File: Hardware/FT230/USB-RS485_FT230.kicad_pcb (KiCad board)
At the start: 2 copper layers, 59 x 22.5 mm, 39 parts, among them J2 7-pin con, J3 5 LVL 3.3, J6 USB_C_Receptacle_USB2.0_16P, Q1 BC857, U1 CH340G, U2 SN75176AD, U3 AMS1117-3.3, U4 DC-DC, U5 EL817, U6 EL817, Y1 12MHz

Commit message: FT230 PCB - in progress
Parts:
- removed Y1: 12MHz, Crystal:Crystal_SMD_3225-4Pin_3.2x2.5mm
- added C5: 100nF, Capacitor_SMD:C_0805_2012Metric, F.Cu at (68.9, 99.9)
- added R7: 10k, Resistor_SMD:R_0805_2012Metric, F.Cu at (71.5, 91.4)
- added R8: 1k, Resistor_SMD:R_0805_2012Metric, F.Cu at (75.8, 96.3)
- C1: value 12pF -> 4.7uF
- C2: value 12pF -> 47pF
- C4: value 100nF -> 47pF
- J2: renamed from J3; value 5 LVL 3.3 -> 3.3 LVL 5
- R1: value 10k -> 27R
- R2: value 1k -> 27R
- U1: value CH340G -> FT230XQ; footprint Package_SO:SOIC-16_3.9x9.9mm_P1.27mm -> Package_DFN_QFN:QFN-16-1EP_4x4mm_P0.65mm_EP2.1x2.1mm
- moved C4 12.0 mm to (65.9, 98.5), turned to 180 degrees
- moved R2 12.0 mm to (65.9, 94.2), turned to 180 degrees
- moved R1 10.5 mm to (65.9, 96.3), turned to 180 degrees
- moved C2 9.04 mm to (65.9, 92.0), turned to 180 degrees
- moved D2 8.06 mm to (71.5, 89.2)
- moved L1 5.46 mm to (75.7, 85.7), turned to 0 degrees
- moved D1 5.33 mm to (73.5, 99.9), turned to -90 degrees
- moved C7 3.48 mm to (77.0, 89.0), turned to 90 degrees
- moved R6 3.15 mm to (74.4, 90.6), turned to 90 degrees
- moved C3 2.63 mm to (65.9, 89.8), turned to 0 degrees
- moved U1 2.45 mm to (70.8, 95.2), turned to -90 degrees
- moved R5 2.41 mm to (75.8, 99.9), turned to -90 degrees
- moved C1 1.44 mm to (71.2, 99.9)
- renumbered C6 to C10, C7 to C6, C8 to C7, C9 to C8, C5 to C9, D4 to D1, D3 to D2, D2 to D3, D1 to D4, J6 to J1, J2 to J3, R12 to R10, R7 to R11, R11 to R12, R9 to R13, R10 to R14, R13 to R15, R6 to R16, R14 to R3, R15 to R4, R3 to R5, R4 to R6, R8 to R9, U5 to U2, U6 to U3, U3 to U5, U2 to U6
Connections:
- C1 pad 2: Net-(U1-XI) -> +5V_USB
- C2 pad 1: GND1 -> Net-(U1-USBDP)
- C2 pad 2: Net-(U1-XO) -> GND1
- C3 pad 1: Net-(U1-V3) -> +5V_USB
- C3 pad 2: +5V_USB -> GND1
- C4 pad 1: +5V_USB -> Net-(U1-USBDM)
- D1 pad 1: Net-(D4-K) -> Net-(D1-K)
- D2 pad 1: Net-(D3-K) -> Net-(D2-K)
- J1 pad A6: Net-(U1-UD+) -> Net-(J1-D+-PadA6)
- J1 pad A7: Net-(U1-UD-) -> Net-(J1-D--PadA7)
- J1 pad B6: Net-(U1-UD+) -> Net-(J1-D+-PadA6)
- J1 pad B7: Net-(U1-UD-) -> Net-(J1-D--PadA7)
- R1 pad 1: +5V_USB -> Net-(U1-USBDM)
- R1 pad 2: Net-(D4-K) -> Net-(J1-D--PadA7)
- R2 pad 1: +5V_USB -> Net-(U1-USBDP)
- R2 pad 2: Net-(R2-Pad2) -> Net-(J1-D+-PadA6)
- R5 pad 1: +5V_USB -> VCCIO
- R6 pad 1: +5V_USB -> VCCIO
- U1 pad 1: GND1 -> VCCIO
- U1 pad 10: unconnected-(U1-~{DSR}-Pad10) -> +5V_USB
- U1 pad 11: unconnected-(U1-~{RI}-Pad11) -> Net-(D1-K)
- U1 pad 13: unconnected-(U1-~{DTR}-Pad13) -> GND1
- U1 pad 15: unconnected-(U1-R232-Pad15) -> Net-(U1-TXD)
- U1 pad 16: +5V_USB -> unconnected-(U1-~{RTS}-Pad16)
- U1 pad 2: Net-(D3-K) -> Net-(U1-RXD)
- U1 pad 3: Net-(D4-K) -> GND1
- U1 pad 4: Net-(U1-V3) -> unconnected-(U1-~{CTS}-Pad4)
- U1 pad 5: Net-(U1-UD+) -> Net-(D2-K)
- U1 pad 6: Net-(U1-UD-) -> Net-(U1-USBDP)
- U1 pad 7: Net-(U1-XI) -> Net-(U1-USBDM)
- U1 pad 8: Net-(U1-XO) -> VCCIO
- U1 pad 9: unconnected-(U1-~{CTS}-Pad9) -> VCCIO
- U2 pad 1: Net-(R2-Pad2) -> Net-(R8-Pad2)
- U2 pad 2: Net-(D3-K) -> Net-(U1-TXD)
- U3 pad 4: Net-(D4-K) -> Net-(U1-RXD)
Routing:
- net Net-(D4-K): track 38.4 -> 0.00 mm
- net Net-(D3-K): track 26.7 -> 0.00 mm
- net GND1: track 89.3 -> 64.6 mm, vias 10 -> 9
- net VCCIO: track 0.00 -> 24.0 mm, vias 0 -> 2
- net +5V_USB: track 52.4 -> 33.4 mm
- net Net-(U1-RXD): track 0.00 -> 16.7 mm
- net Net-(U1-TXD): track 0.00 -> 13.5 mm
- net Net-(U1-V3): track 9.47 -> 0.00 mm
- net Net-(U1-XO): track 8.45 -> 0.00 mm
- net Net-(R8-Pad2): track 0.00 -> 7.80 mm
- net Net-(U1-XI): track 7.73 -> 0.00 mm
- net Net-(U1-UD-): track 7.16 -> 0.00 mm, vias 2 -> 0
- net Net-(U1-UD+): track 6.73 -> 0.00 mm
- net Net-(J1-D--PadA7): track 0.00 -> 6.21 mm, vias 0 -> 2
- net Net-(D2-K): track 0.00 -> 5.86 mm
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
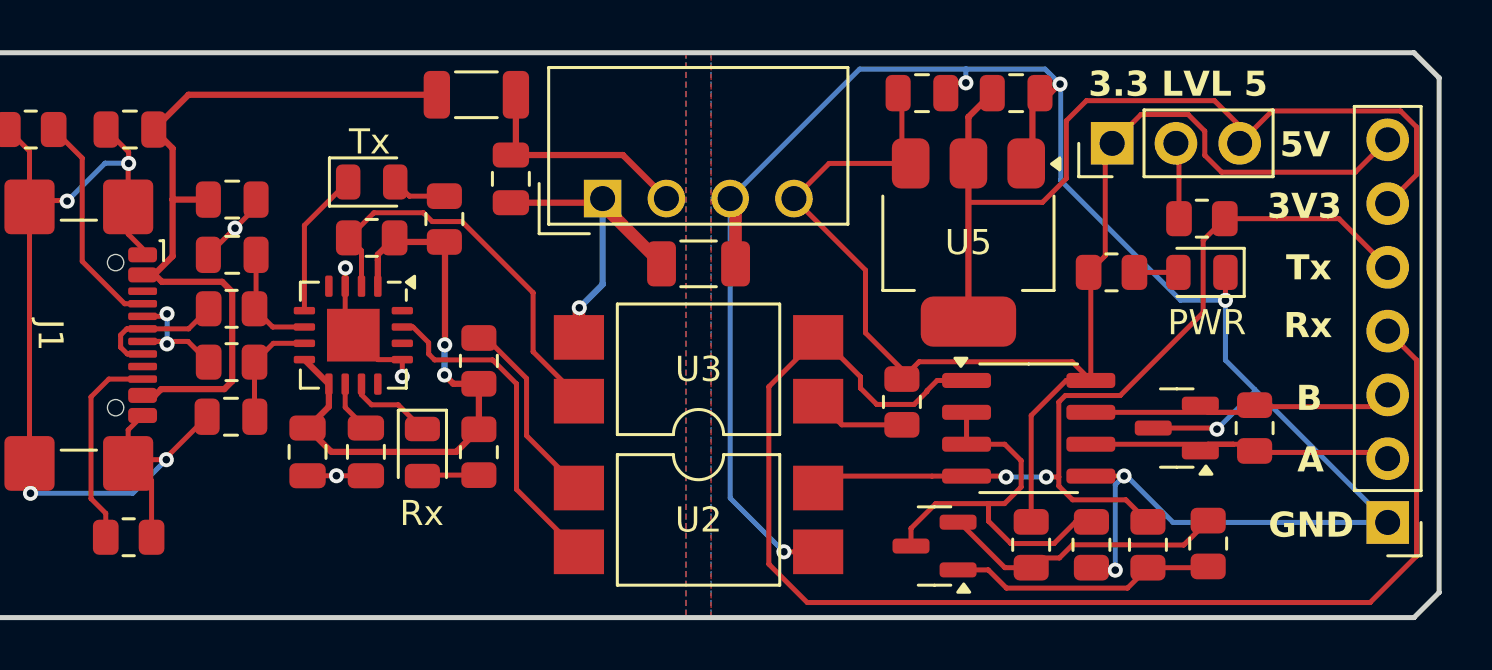
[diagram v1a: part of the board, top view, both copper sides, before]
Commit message: FT230 BOM and fix
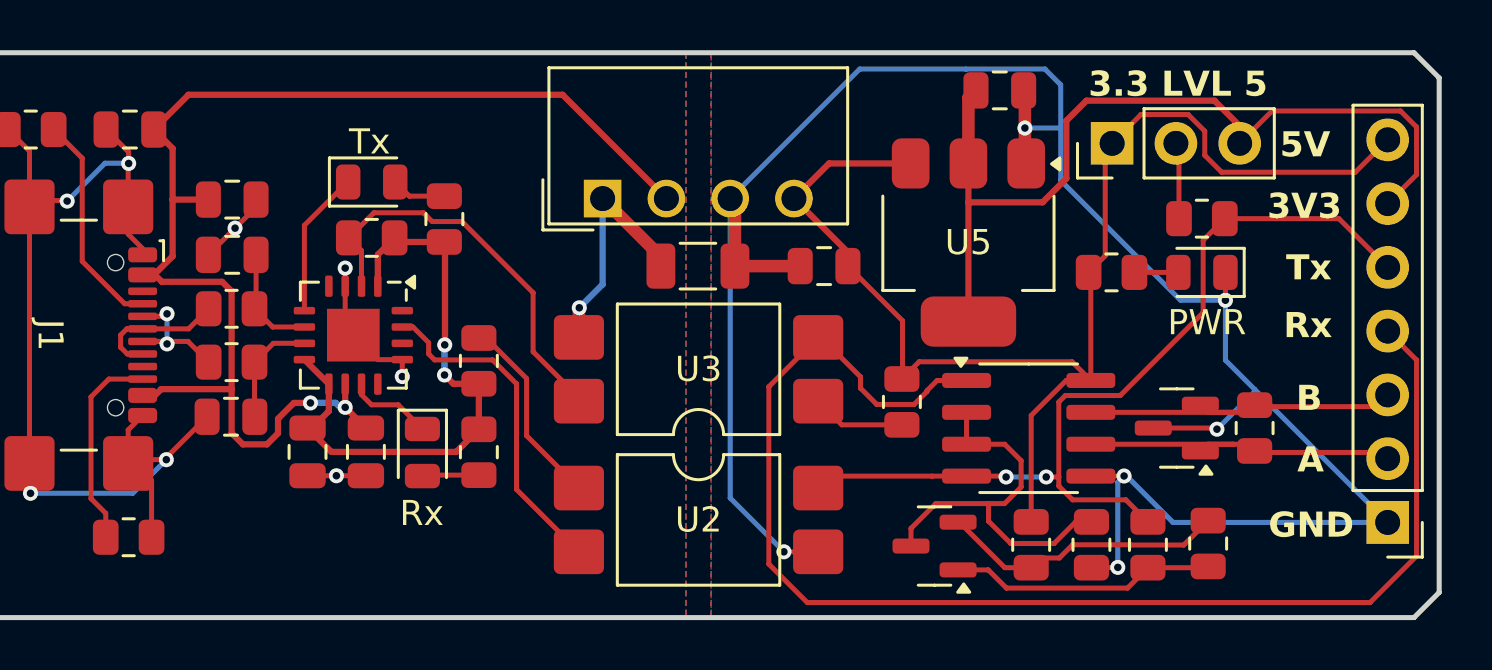
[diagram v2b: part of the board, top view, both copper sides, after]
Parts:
- removed C10: 22uF, Capacitor_SMD:C_0805_2012Metric
- removed L1: 6.8uH, Inductor_SMD:L_1206_3216Metric
- C7: value 4.7uF -> 270pF/2kV; footprint Capacitor_SMD:C_0805_2012Metric -> Capacitor_SMD:C_1206_3216Metric
- C8: value 270pF/2kV -> 10uF; footprint Capacitor_SMD:C_1206_3216Metric -> Capacitor_SMD:C_0805_2012Metric
- C9: value 10uF -> 22uF
- U6: value SN75176AD -> SN75176
- moved C7 8.22 mm to (84.5, 92.5), turned to 0 degrees
- moved C8 5.00 mm to (89.5, 92.5)
- moved C9 3.10 mm to (96.5, 85.5)
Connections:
- C7 pad 2: Net-(U4-+Vin) -> GND2
- C8 pad 1: GND1 -> GND2
- C8 pad 2: GND2 -> +5V_OUT
- C9 pad 2: +5V_OUT -> +3.3V_OUT
- U4 pad 2: Net-(U4-+Vin) -> +5V_USB
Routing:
- net +5V_USB: track 33.4 -> 52.0 mm, vias 0 -> 2
- net Net-(U4-+Vin): track 9.40 -> 0.00 mm
- net GND1: track 64.6 -> 60.9 mm
- net +5V_OUT: track 55.9 -> 52.9 mm
- net GND2: track 87.3 -> 88.8 mm, vias 7 -> 6
- net +3.3V_OUT: track 36.7 -> 35.5 mm

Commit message: FT230 gerbers export
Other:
- board text added: "USB-UART/RS485 (GALVANIC ISOLATION)"
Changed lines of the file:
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@@
+		)
+	)
+	(gr_text "USB-UART/RS485 (GALVANIC ISOLATION)"
+		(at 87.45 86.45 0)
+		(layer "B.SilkS")
+		(effects
+			(font
+				(size 1 1)
+				(thickness 0.25)
+				(bold yes)
+			)
+			(justify left bottom mirror)
 		)
 	)

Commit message: -opto +Adum & 1.8
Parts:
- removed C9: 22uF, Capacitor_SMD:C_0805_2012Metric
- removed J2: 3.3 LVL 5, Connector_PinHeader_2.54mm:PinHeader_1x03_P2.54mm_Vertical
- removed R7: 10k, Resistor_SMD:R_0805_2012Metric
- removed R8, R9: 1k, Resistor_SMD:R_0805_2012Metric
- removed U2, U3: EL817, Package_DIP:SMDIP-4_W9.53mm
- added C10: 100nF, Capacitor_SMD:C_0805_2012Metric, F.Cu at (62.2, 77.1)
- added J4: Conn_02x03_Odd_Even, Connector_PinHeader_1.00mm:PinHeader_2x03_P1.00mm_Vertical, F.Cu at (57.3, 77.1)
- added U7: ADuM121N, Package_SO:SOIC-8_3.9x4.9mm_P1.27mm, F.Cu at (59.9, 72.4)
- D1: value Rx -> Tx
- D2: value Tx -> Rx
- U5: value AMS1117-3.3 -> AP7345D-1833RH4-7; footprint Package_TO_SOT_SMD:SOT-223-3_TabPin2 -> AP7345D-1833:AP7345D1833RH47
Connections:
- C7 pad 2: GND2 -> Net-(U4--Vout)
- C8 pad 1: GND2 -> Net-(U4--Vout)
- R11 pad 2: Net-(J2-Pin_2) -> unconnected-(R11-Pad2)
- U4 pad 3: GND2 -> Net-(U4--Vout)
- U5 pad 2: +3.3V_OUT -> +1.8V
- U5 pad 3: +5V_OUT -> +3.3V
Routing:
- net (no net): track 0.00 -> 11.5 mm
- net Net-(R8-Pad2): track 7.80 -> 0.00 mm
- net Net-(R9-Pad2): track 3.73 -> 0.00 mm
- net unconnected-(R11-Pad2): track 0.00 -> 3.05 mm
- net Net-(J2-Pin_2): track 3.05 -> 0.00 mm

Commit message: schematics change
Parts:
- removed J3: 7-pin con, Connector_PinHeader_2.54mm:PinHeader_1x07_P2.54mm_Vertical
- removed Q1: BC857, Package_TO_SOT_SMD:SOT-23
- removed R10, R14: 100R, Resistor_SMD:R_0805_2012Metric
- removed R11, R12, R13: 10k, Resistor_SMD:R_0805_2012Metric
- removed R15: 120R, Resistor_SMD:R_0805_2012Metric
- removed R16: 1k, Resistor_SMD:R_0805_2012Metric
- removed U6: SN75176, Package_SO:SOIC-8_3.9x4.9mm_P1.27mm
- removed U7: ADuM121N, Package_SO:SOIC-8_3.9x4.9mm_P1.27mm
- added C11: 10uF, Capacitor_SMD:C_0805_2012Metric, F.Cu at (83.0, 58.0)
- added C12: 100nF, Capacitor_SMD:C_0805_2012Metric, F.Cu at (83.0, 61.0)
- added C13: 100nF, Capacitor_SMD:C_0805_2012Metric, F.Cu at (83.0, 64.0)
- added C14: 100nF, Capacitor_SMD:C_0805_2012Metric, F.Cu at (83.0, 67.0)
- added C15: 100nF, Capacitor_SMD:C_0805_2012Metric, F.Cu at (83.0, 70.0)
- added C9: 270pF/2kV, Capacitor_SMD:C_1206_3216Metric, F.Cu at (95.7, 58.2)
- added J2: 7-pin con, Connector_PinHeader_2.54mm:PinHeader_1x07_P2.54mm_Vertical, F.Cu at (72.9, 56.8)
- added R7: 120R, Resistor_SMD:R_0805_2012Metric, F.Cu at (95.9, 71.3)
- added R8: 1k, Resistor_SMD:R_0805_2012Metric, F.Cu at (95.9, 74.3)
- added U2: ADuM121N, Package_SO:SOIC-8_3.9x4.9mm_P1.27mm, F.Cu at (113.6, 63.6)
- added U3: DC-DC, Converter_DCDC:Converter_DCDC_TRACO_TEA1-xxxx_THT, F.Cu at (110.2, 59.8)
- C7: value 270pF/2kV -> 100nF; footprint Capacitor_SMD:C_1206_3216Metric -> Capacitor_SMD:C_0805_2012Metric
- C8: value 10uF -> 100nF
- J4: value Conn_02x03_Odd_Even -> Conn_02x04_Odd_Even
- U4: value DC-DC -> ISO3082DW; footprint Converter_DCDC:Converter_DCDC_TRACO_TEA1-xxxx_THT -> Package_SO:SOIC-16W_7.5x10.3mm_P1.27mm
- moved C7 52.2 mm to (135.7, 82.5)
- moved U4 37.4 mm to (113.6, 72.0), turned to 0 degrees
- moved C8 36.9 mm to (126.3, 90.7)
- moved U5 30.7 mm to (125.2, 84.5)
- moved D3 23.9 mm to (118.8, 80.6)
- moved D4 14.5 mm to (118.5, 88.9)
- moved J4 12.4 mm to (58.0, 64.7)
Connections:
- C10 pad 1: GND1 -> +V_OUT
- C10 pad 2: VCCIO -> GND2
- C7 pad 2: Net-(U4--Vout) -> Net-(U4-Vcc1)
- C8 pad 1: Net-(U4--Vout) -> GND1
- C8 pad 2: +5V_OUT -> VCCIO
- J4 pad 1: unconnected-(J4-Pin_1-Pad1) -> +1.8V_ISO
- J4 pad 2: unconnected-(J4-Pin_2-Pad2) -> +V_OUT
- J4 pad 3: unconnected-(J4-Pin_3-Pad3) -> +3.3V_ISO
- J4 pad 4: unconnected-(J4-Pin_4-Pad4) -> +V_OUT
- J4 pad 5: unconnected-(J4-Pin_5-Pad5) -> +5V_ISO
- J4 pad 6: unconnected-(J4-Pin_6-Pad6) -> +V_OUT
- U1 pad 11: Net-(D1-K) -> Net-(D2-K)
- U1 pad 12: unconnected-(U1-CBUS0-Pad12) -> Net-(D1-K)
- U1 pad 14: unconnected-(U1-CBUS3-Pad14) -> Net-(U1-CBUS3)
- U1 pad 5: Net-(D2-K) -> Net-(U1-CBUS2)
- U4 pad 1: GND1 -> Net-(U4-Vcc1)
- U4 pad 2: +5V_USB -> GND1
- U4 pad 3: Net-(U4--Vout) -> Net-(U1-RXD)
- U4 pad 4: +5V_OUT -> Net-(U1-CBUS3)
- U5 pad 2: +1.8V -> +1.8V_ISO
- U5 pad 3: +3.3V -> +3.3V_ISO
- U5 pad 5: +5V_OUT -> +5V_ISO
- U5 pad 6: +5V_OUT -> +5V_ISO
- U5 pad 7: +5V_OUT -> +5V_ISO
- U5 pad 8: +5V_OUT -> +5V_ISO
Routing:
- net GND2: track 88.8 -> 0.00 mm, vias 6 -> 0
- net Net-(J3-Pin_4): track 54.2 -> 0.00 mm
- net +5V_OUT: track 52.9 -> 0.00 mm
- net Net-(J3-Pin_5): track 36.9 -> 0.00 mm, vias 2 -> 0
- net +3.3V_OUT: track 35.5 -> 0.00 mm
- net +5V_USB: track 52.0 -> 31.3 mm
- net Net-(Q1-C): track 16.1 -> 0.00 mm
- net Net-(D3-A2): track 13.6 -> 0.00 mm
- net Net-(D3-A1): track 13.5 -> 0.00 mm
- net (no net): track 11.5 -> 0.00 mm
- net Net-(Q1-E): track 11.5 -> 0.00 mm
- net Net-(Q1-B): track 10.6 -> 0.00 mm
- net GND1: track 60.9 -> 51.4 mm, vias 9 -> 8
- net Net-(U1-RXD): track 16.7 -> 11.6 mm
- net Net-(U1-TXD): track 13.5 -> 9.96 mm
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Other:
- board text removed: "3V3"
- board text removed: "5V"
- board text removed: "A"
- board text removed: "B"
- board text removed: "GND"
- board text removed: "Rx"
- board text removed: "Tx"

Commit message: Schematics update
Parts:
- J4: footprint Connector_PinHeader_1.00mm:PinHeader_2x03_P1.00mm_Vertical -> Connector_PinHeader_2.54mm:PinHeader_2x04_P2.54mm_Vertical
- moved J4 1.57 mm to (56.5, 64.3)
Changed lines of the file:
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@@
 	(net 34 "unconnected-(U4-NC-Pad11)")
 	(net 35 "unconnected-(U4-NC-Pad14)")
+	(net 36 "VCC_485")
 	(footprint "Package_TO_SOT_SMD:SOT-23"
 		(layer "F.Cu")
@@
 		)
 	)
-	(footprint "Connector_PinHeader_1.00mm:PinHeader_2x03_P1.00mm_Vertical"
+	(footprint "Connector_PinHeader_2.54mm:PinHeader_2x04_P2.54mm_Vertical"
 		(layer "F.Cu")
-		(at 57.96 64.74)
-		(descr "Through hole straight pin header, 2x03, 1.00mm pitch, double rows")
-		(tags "Through hole pin header THT 2x03 1.00mm double row")
+		(at 56.46 64.27)
+		(descr "Through hole straight pin header, 2x04, 2.54mm pitch, double rows")
+		(tags "Through hole pin header THT 2x04 2.54mm double row")
 		(property "Reference" "J4"
-			(at 0.5 -1.61 0)
+			(at 1.27 -2.38 0)
 			(layer "F.SilkS")
 			(effects
@@
 		)
 		(property "Value" "Conn_02x04_Odd_Even"
-			(at 0.5 3.61 0)
+			(at 1.27 10 0)
 			(layer "F.Fab")
 			(effects
@@
 		(attr through_hole)
 		(fp_line
-			(start -0.76 -0.735)
-			(end 0 -0.735)
-			(stroke
-				(width 0.12)
-				(type solid)
-			)
-			(layer "F.SilkS")
-		)
-		(fp_line
-			(start -0.76 0)
-			(end -0.76 -0.735)
-			(stroke
-				(width 0.12)
-				(type solid)
-			)
-			(layer "F.SilkS")
-		)
-		(fp_line
-			(start -0.76 0.735)
-			(end -0.76 2.61)
-			(stroke
-				(width 0.12)
-				(type solid)
-			)
-			(layer "F.SilkS")
-		)
-		(fp_line
-			(start -0.76 0.735)
-			(end -0.685565 0.735)
-			(stroke
-				(width 0.12)
-				(type solid)
-			)
-			(layer "F.SilkS")
-		)
-		(fp_line
-			(start -0.76 2.61)
-			(end -0.41003 2.61)
-			(stroke
-				(width 0.12)
-				(type solid)
-			)
-			(layer "F.SilkS")
-		)
-		(fp_line
-			(start 0.41003 2.61)
-			(end 0.58997 2.61)
-			(stroke
-				(width 0.12)
-				(type solid)
-			)
-			(layer "F.SilkS")
-		)
-		(fp_line
-			(start 1.41003 -0.61)
-			(end 1.76 -0.61)
-			(stroke
-				(width 0.12)
-				(type solid)
-			)
-			(layer "F.SilkS")
-		)
-		(fp_line
-			(start 1.41003 2.61)
-			(end 1.76 2.61)
-			(stroke
-				(width 0.12)
-				(type solid)
-			)
-			(layer "F.SilkS")
-		)
-		(fp_line
-			(start 1.76 -0.61)
-			(end 1.76 2.61)
-			(stroke
-				(width 0.12)
-				(type solid)
-			)
-			(layer "F.SilkS")
-		)
-		(fp_line
-			(start -1.15 -1)
-			(end -1.15 3)
-			(stroke
-				(width 0.05)
-				(type solid)
-			)
-			(layer "F.CrtYd")
-		)
-		(fp_line
-			(start -1.15 3)
-			(end 2.15 3)
-			(stroke
-				(width 0.05)
-				(type solid)
-			)
-			(layer "F.CrtYd")
-		)
-		(fp_line
-			(start 2.15 -1)
-			(end -1.15 -1)
-			(stroke
-				(width 0.05)
-				(type solid)
-			)
-			(layer "F.CrtYd")
-		)
-		(fp_line
-			(start 2.15 3)
-			(end 2.15 -1)
-			(stroke
-				(width 0.05)
-				(type solid)
-			)
-			(layer "F.CrtYd")
-		)
-		(fp_line
-			(start -0.65 0.075)
-			(end -0.075 -0.5)
-			(stroke
-				(width 0.1)
-				(type solid)
-			)
-			(layer "F.Fab")
-		)
-		(fp_line
-			(start -0.65 2.5)
-			(end -0.65 0.075)
-			(stroke
-				(width 0.1)
-				(type solid)
-			)
-			(layer "F.Fab")
-		)
-		(fp_line
-			(start -0.075 -0.5)
-			(end 1.65 -0.5)
-			(stroke
-				(width 0.1)
-				(type solid)
-			)
-			(layer "F.Fab")
-		)
-		(fp_line
-			(start 1.65 -0.5)
-			(end 1.65 2.5)
-			(stroke
-				(width 0.1)
-				(type solid)
-			)
-			(layer "F.Fab")
-		)
-		(fp_line
-			(start 1.65 2.5)
-			(end -0.65 2.5)
+			(start -1.38 -1.38)
+			(end 0 -1.38)
+			(stroke
+				(width 0.12)
+				(type solid)
+			)
+			(layer "F.SilkS")
+		)
+		(fp_line
+			(start -1.38 0)
+			(end -1.38 -1.38)
+			(stroke
+				(width 0.12)
+				(type solid)
+			)
+			(layer "F.SilkS")
+		)
+		(fp_line
+			(start -1.38 1.27)
+			(end -1.38 9)
+			(stroke
+				(width 0.12)
+				(type solid)
+			)
+			(layer "F.SilkS")
+		)
+		(fp_line
+			(start -1.38 1.27)
+			(end 1.27 1.27)
+			(stroke
+				(width 0.12)
+				(type solid)
+			)
+			(layer "F.SilkS")
+		)
+		(fp_line
+			(start -1.38 9)
+			(end 3.92 9)
+			(stroke
+				(width 0.12)
+				(type solid)
+			)
+			(layer "F.SilkS")
+		)
+		(fp_line
+			(start 1.27 -1.38)
+			(end 3.92 -1.38)
+			(stroke
+				(width 0.12)
+				(type solid)
+			)
+			(layer "F.SilkS")
+		)
+		(fp_line
+			(start 1.27 1.27)
+			(end 1.27 -1.38)
+			(stroke
+				(width 0.12)
+				(type solid)
+			)
+			(layer "F.SilkS")
+		)
+		(fp_line
+			(start 3.92 -1.38)
+			(end 3.92 9)
+			(stroke
+				(width 0.12)
+				(type solid)
+			)
+			(layer "F.SilkS")
+		)
+		(fp_line
+			(start -1.77 -1.77)
+			(end -1.77 9.39)
+			(stroke
+				(width 0.05)
+				(type solid)
+			)
+			(layer "F.CrtYd")
+		)
+		(fp_line
+			(start -1.77 9.39)
+			(end 4.32 9.39)
+			(stroke
+				(width 0.05)
+				(type solid)
+			)
+			(layer "F.CrtYd")
+		)
+		(fp_line
+			(start 4.32 -1.77)
+			(end -1.77 -1.77)
+			(stroke
+				(width 0.05)
+				(type solid)
+			)
+			(layer "F.CrtYd")
+		)
+		(fp_line
+			(start 4.32 9.39)
+			(end 4.32 -1.77)
+			(stroke
+				(width 0.05)
+				(type solid)
+			)
+			(layer "F.CrtYd")
+		)
+		(fp_line
+			(start -1.27 0)
+			(end 0 -1.27)
+			(stroke
+				(width 0.1)
+				(type solid)
+			)
+			(layer "F.Fab")
+		)
+		(fp_line
+			(start -1.27 8.89)
+			(end -1.27 0)
+			(stroke
+				(width 0.1)
+				(type solid)
+			)
+			(layer "F.Fab")
+		)
+		(fp_line
+			(start 0 -1.27)
+			(end 3.81 -1.27)
+			(stroke
+				(width 0.1)
+				(type solid)
+			)
+			(layer "F.Fab")
+		)
+		(fp_line
+			(start 3.81 -1.27)
+			(end 3.81 8.89)
+			(stroke
+				(width 0.1)
+				(type solid)
+			)
+			(layer "F.Fab")
+		)
+		(fp_line
+			(start 3.81 8.89)
+			(end -1.27 8.89)
 			(stroke
 				(width 0.1)
@@
 		)
 		(fp_text user "${REFERENCE}"
-			(at 0.5 1 90)
+			(at 1.27 3.81 90)
 			(layer "F.Fab")
 			(effects
@@
 		(pad "1" thru_hole rect
 			(at 0 0)
-			(size 0.85 0.85)
-			(drill 0.5)
+			(size 1.7 1.7)
+			(drill 1)
 			(layers "*.Cu" "*.Mask")
 			(remove_unused_layers no)
@@
 		)
 		(pad "2" thru_hole circle
-			(at 1 0)
-			(size 0.85 0.85)
-			(drill 0.5)
+			(at 2.54 0)
+			(size 1.7 1.7)
+			(drill 1)
 			(layers "*.Cu" "*.Mask")
 			(remove_unused_layers no)
@@
 		)
 		(pad "3" thru_hole circle
-			(at 0 1)
-			(size 0.85 0.85)
-			(drill 0.5)
+			(at 0 2.54)
+			(size 1.7 1.7)
+			(drill 1)
 			(layers "*.Cu" "*.Mask")
 			(remove_unused_layers no)
@@
 		)
 		(pad "4" thru_hole circle
-			(at 1 1)
-			(size 0.85 0.85)
-			(drill 0.5)
+			(at 2.54 2.54)
+			(size 1.7 1.7)
+			(drill 1)
 			(layers "*.Cu" "*.Mask")
 			(remove_unused_layers no)
@@
 		)
 		(pad "5" thru_hole circle
-			(at 0 2)
-			(size 0.85 0.85)
-			(drill 0.5)
+			(at 0 5.08)
+			(size 1.7 1.7)
+			(drill 1)
 			(layers "*.Cu" "*.Mask")
 			(remove_unused_layers no)
@@
 		)
 		(pad "6" thru_hole circle
-			(at 1 2)
-			(size 0.85 0.85)
-			(drill 0.5)
+			(at 2.54 5.08)
+			(size 1.7 1.7)
+			(drill 1)
 			(layers "*.Cu" "*.Mask")
 			(remove_unused_layers no)
@@
 			(pintype "passive")
 		)
+		(pad "7" thru_hole circle
+			(at 0 7.62)
+			(size 1.7 1.7)
+			(drill 1)
+			(layers "*.Cu" "*.Mask")
+			(remove_unused_layers no)
+			(net 9 "VCCIO")
+			(pinfunction "Pin_7")
+			(pintype "passive")
+		)
+		(pad "8" thru_hole circle
+			(at 2.54 7.62)
+			(size 1.7 1.7)
+			(drill 1)
+			(layers "*.Cu" "*.Mask")
+			(remove_unused_layers no)
+			(net 36 "VCC_485")
+			(pinfunction "Pin_8")
+			(pintype "passive")
+		)
 		(embedded_fonts no)
-		(model "${KICAD9_3DMODEL_DIR}/Connector_PinHeader_1.00mm.3dshapes/PinHeader_2x03_P1.00mm_Vertical.step"
+		(model "${KICAD9_3DMODEL_DIR}/Connector_PinHeader_2.54mm.3dshapes/PinHeader_2x04_P2.54mm_Vertical.step"
 			(offset
 				(xyz 0 0 0)
